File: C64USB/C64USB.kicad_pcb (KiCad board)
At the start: 2 copper layers, 39.3 x 64.2 mm, 32 parts, among them J2 USB_B, J3 AVR-ISP-6, J4 Joystick1, J5 Joystick2, J6 LED, U2 ATmega88-20A, Y1 16MHz

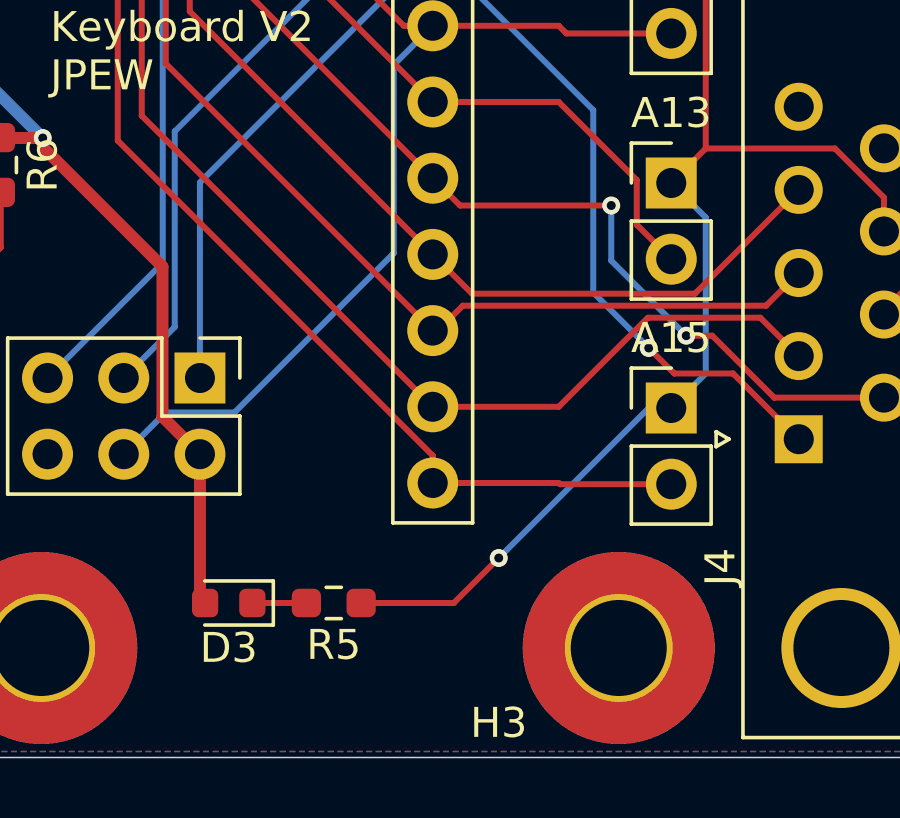
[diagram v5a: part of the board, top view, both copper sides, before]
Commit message: Remove debug LED
The debug LED isn't particularly useful since it's tied to the AUX line
and I didn't even bother populating it on the prototype board
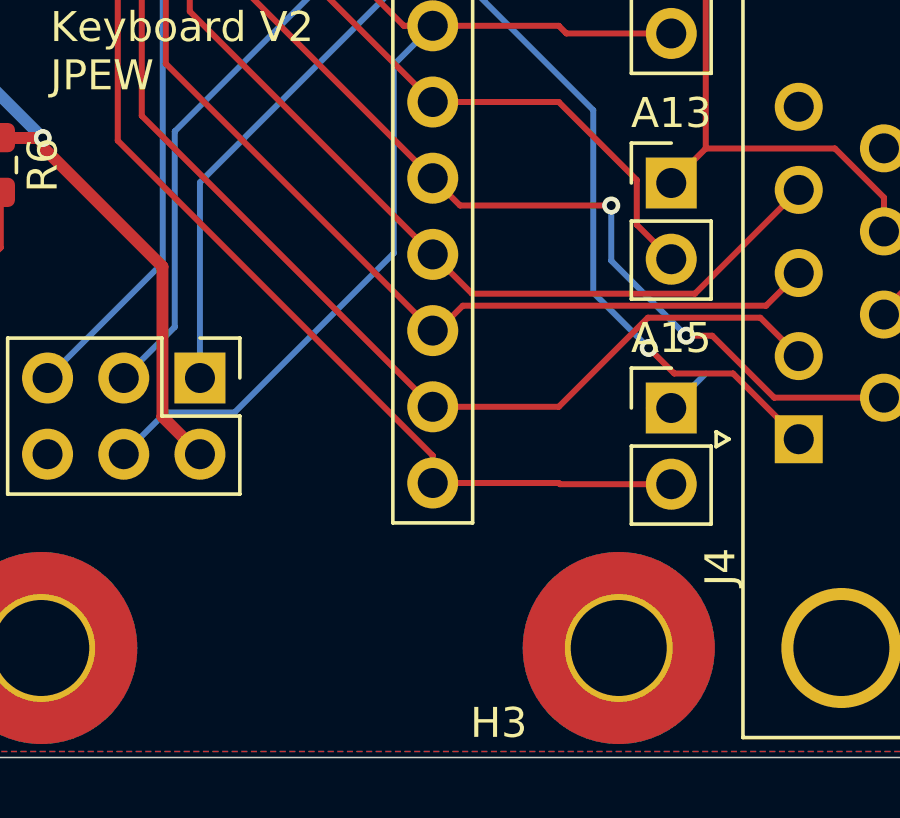
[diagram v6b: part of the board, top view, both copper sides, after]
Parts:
- removed D3: LED, LED_SMD:LED_0603_1608Metric
- removed R5: 120, Resistor_SMD:R_0603_1608Metric_Pad0.98x0.95mm_HandSolder
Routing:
- net /AUX: track 96.5 -> 77.4 mm, vias 2 -> 1
- net /PWR: track 143.7 -> 138.7 mm
- net Net-(D3-K): track 1.80 -> 0.00 mm

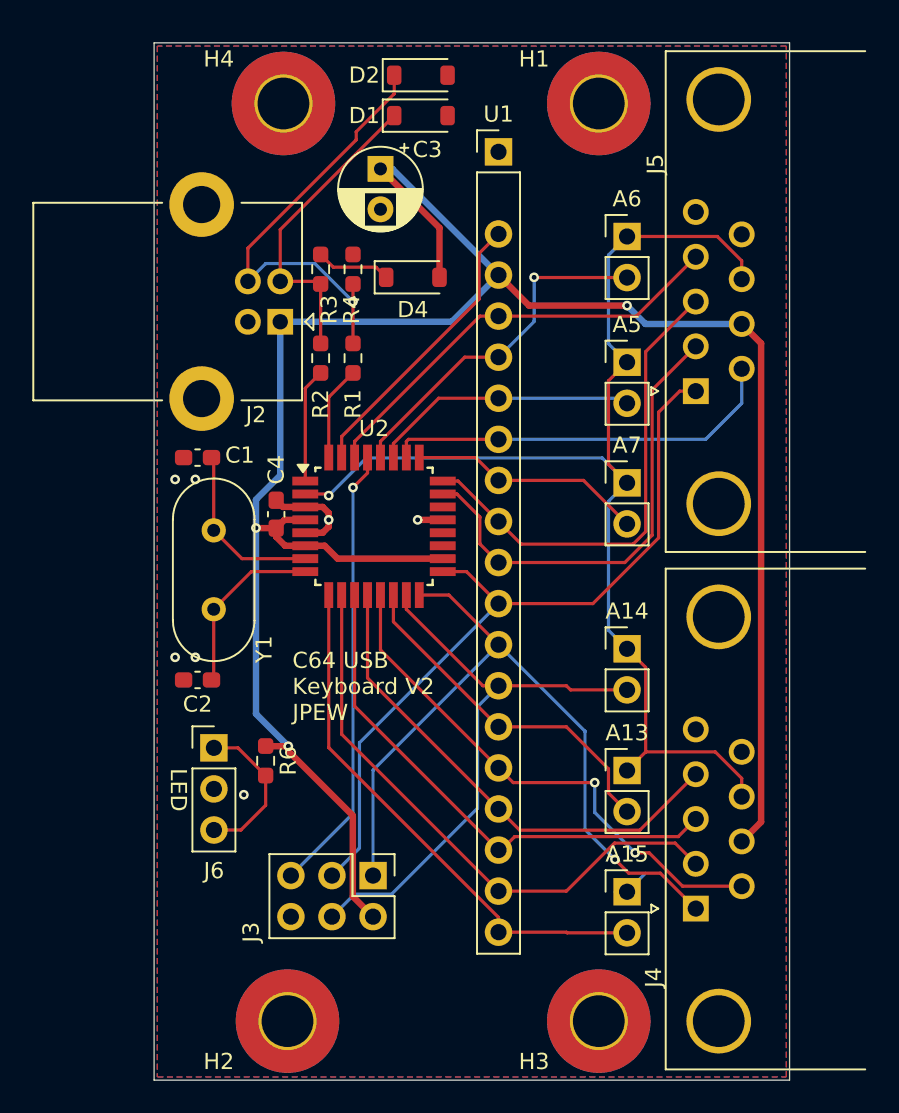
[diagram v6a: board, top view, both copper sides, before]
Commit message: Move mounting holes
Moves the mounting holes to a better position
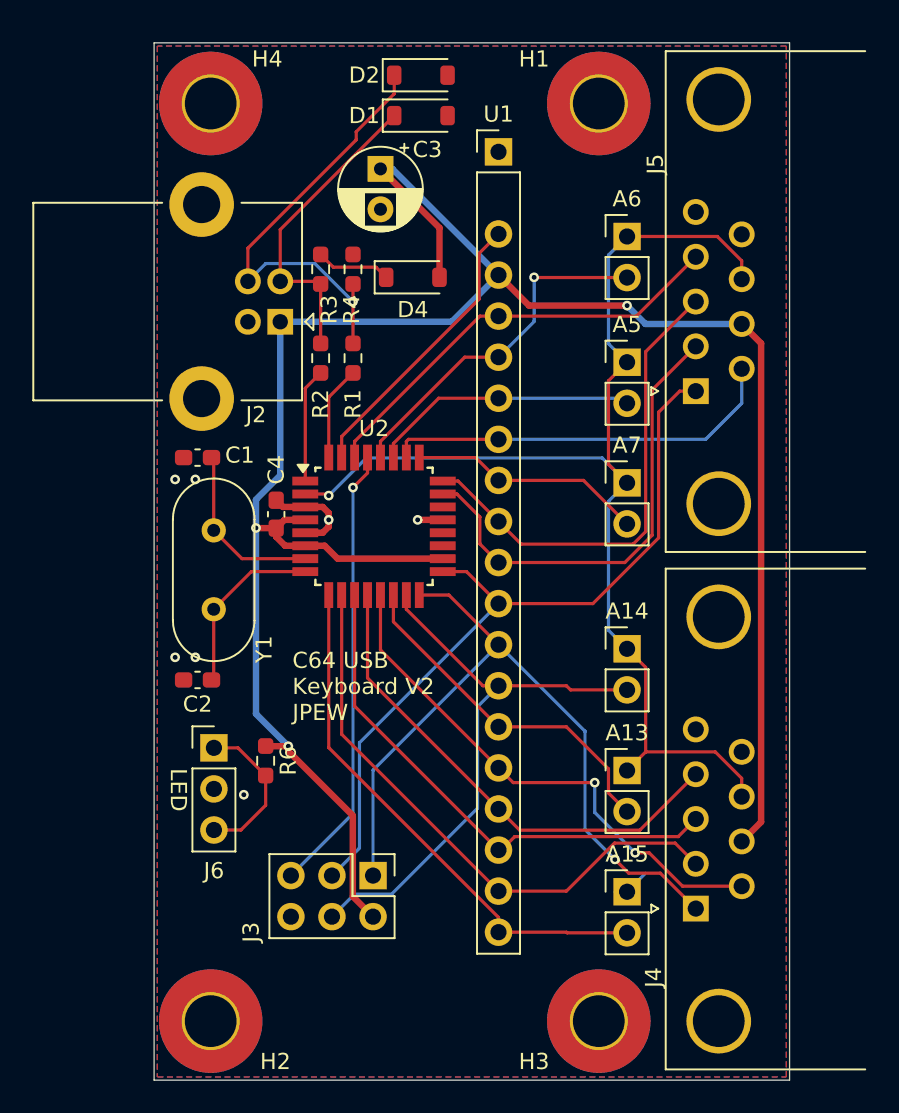
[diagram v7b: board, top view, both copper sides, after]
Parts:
- moved H2 4.75 mm to (117.0, 113.5)
- moved H4 4.50 mm to (117.0, 56.8)
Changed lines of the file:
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@@
 	(footprint "MountingHole:MountingHole_3.2mm_M3_Pad_TopBottom"
 		(layer "F.Cu")
-		(at 121.5 56.75)
+		(at 117 56.75)
 		(descr "Mounting Hole 3.2mm, M3")
 		(tags "mounting hole 3.2mm m3")
 		(property "Reference" "H4"
-			(at -4 -2.75 0)
+			(at 3.5 -2.75 0)
 			(layer "F.SilkS")
 			(effects
@@
 	(footprint "MountingHole:MountingHole_3.2mm_M3_Pad_TopBottom"
 		(layer "F.Cu")
-		(at 121.75 113.5)
+		(at 117 113.5)
 		(descr "Mounting Hole 3.2mm, M3")
 		(tags "mounting hole 3.2mm m3")
 		(property "Reference" "H2"
-			(at -4.25 2.5 0)
-			(layer "F.SilkS")
-			(effects
+			(at 4 2.5 0)
+			(layer "F.SilkS")
+			(effects

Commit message: Use buffer on joystick and aux keys
There was a problem where joystick or auxiliary key inputs would result
in keyboard keys being detected when they were not actually pressed.
While this is accurate to the actual Commodore 64 keyboard and joystick
input, having it happen on this USB device meant that it could not be
correctly disambiguated by the emulator. As such, the board is
redesigned to use a 74HCT541 tri state buffer chip to isolate the
Joystick and auxiliary inputs from the keyboard. It is still possible
that keyboard inputs can incorrectly show up as joystick movement, but
this is much less likely to cause a problem.

With the board redesign, the clearance around the keyboard header was
also increased to allow it to fit, and the USB connector was changed
from a micro-USB connector to a USB-B connector (I had too much trouble
hand soldering the micro USB connector).
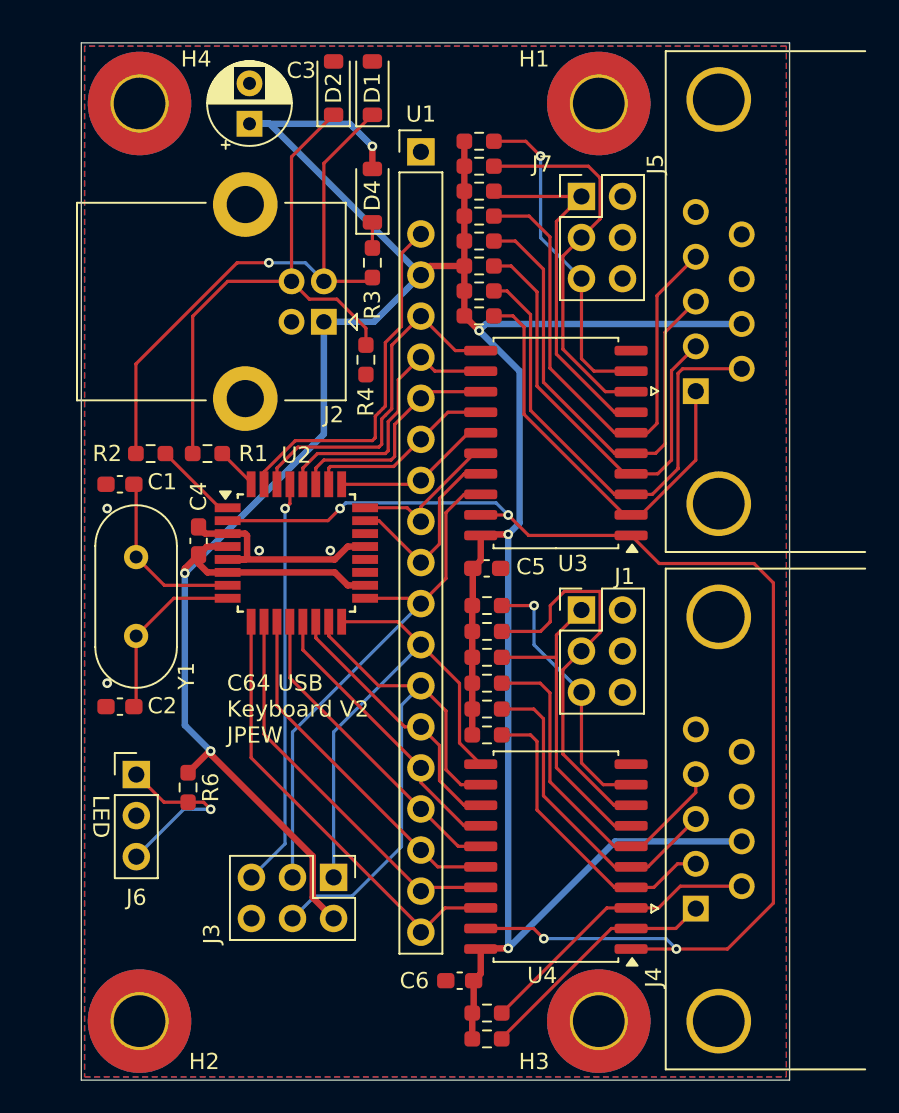
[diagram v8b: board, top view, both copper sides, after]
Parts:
- removed A13, A14, A15, A5, A6, A7: ~, Connector_PinHeader_2.54mm:PinHeader_1x02_P2.54mm_Vertical
- added C5: 100nF, Capacitor_SMD:C_0603_1608Metric_Pad1.08x0.95mm_HandSolder, F.Cu at (134.1, 85.5)
- added C6: 100nF, Capacitor_SMD:C_0603_1608Metric_Pad1.08x0.95mm_HandSolder, F.Cu at (132.4, 111.0)
- added J1: Conn_02x03_Odd_Even, Connector_PinHeader_2.54mm:PinHeader_2x03_P2.54mm_Vertical, F.Cu at (139.9, 88.1)
- added J7: Conn_02x03_Odd_Even, Connector_PinHeader_2.54mm:PinHeader_2x03_P2.54mm_Vertical, F.Cu at (139.9, 62.5)
- added R10: 10k, Resistor_SMD:R_0603_1608Metric_Pad0.98x0.95mm_HandSolder, F.Cu at (133.6, 63.7)
- added R11: 10k, Resistor_SMD:R_0603_1608Metric_Pad0.98x0.95mm_HandSolder, F.Cu at (133.6, 62.2)
- added R12: 10k, Resistor_SMD:R_0603_1608Metric_Pad0.98x0.95mm_HandSolder, F.Cu at (133.6, 60.6)
- added R13: 10k, Resistor_SMD:R_0603_1608Metric_Pad0.98x0.95mm_HandSolder, F.Cu at (133.6, 59.1)
- added R14: 10k, Resistor_SMD:R_0603_1608Metric_Pad0.98x0.95mm_HandSolder, F.Cu at (134.1, 114.6)
- added R15: 10k, Resistor_SMD:R_0603_1608Metric_Pad0.98x0.95mm_HandSolder, F.Cu at (134.1, 113.0)
- added R16: 10k, Resistor_SMD:R_0603_1608Metric_Pad0.98x0.95mm_HandSolder, F.Cu at (134.1, 95.8)
- added R17: 10k, Resistor_SMD:R_0603_1608Metric_Pad0.98x0.95mm_HandSolder, F.Cu at (134.1, 94.2)
- added R18: 10k, Resistor_SMD:R_0603_1608Metric_Pad0.98x0.95mm_HandSolder, F.Cu at (134.1, 92.6)
- added R19: 10k, Resistor_SMD:R_0603_1608Metric_Pad0.98x0.95mm_HandSolder, F.Cu at (134.1, 91.0)
- added R20: 10k, Resistor_SMD:R_0603_1608Metric_Pad0.98x0.95mm_HandSolder, F.Cu at (134.1, 89.4)
- added R21: 10k, Resistor_SMD:R_0603_1608Metric_Pad0.98x0.95mm_HandSolder, F.Cu at (134.1, 87.8)
- added R5: 10k, Resistor_SMD:R_0603_1608Metric_Pad0.98x0.95mm_HandSolder, F.Cu at (133.6, 69.9)
- added R7: 10k, Resistor_SMD:R_0603_1608Metric_Pad0.98x0.95mm_HandSolder, F.Cu at (133.6, 66.8)
- added R8: 10k, Resistor_SMD:R_0603_1608Metric_Pad0.98x0.95mm_HandSolder, F.Cu at (133.6, 68.3)
- added R9: 10k, Resistor_SMD:R_0603_1608Metric_Pad0.98x0.95mm_HandSolder, F.Cu at (133.6, 65.3)
- added U3: 74HCT541, Package_SO:SOIC-20W_7.5x12.8mm_P1.27mm, F.Cu at (138.3, 77.7)
- added U4: 74HCT541, Package_SO:SOIC-20W_7.5x12.8mm_P1.27mm, F.Cu at (138.3, 103.3)
- moved R2 12.1 mm to (113.3, 78.4), turned to 180 degrees
- moved R1 10.8 mm to (116.8, 78.4), turned to 180 degrees
- moved C3 8.57 mm to (119.4, 58.0), turned to 90 degrees
- moved R4 5.66 mm to (126.6, 72.6), turned to 90 degrees
- moved D4 5.63 mm to (127.0, 62.5), turned to 90 degrees
- moved D2 5.46 mm to (124.6, 55.8), turned to 90 degrees
- moved R6 5.08 mm to (115.6, 99.0)
- moved J6 5.08 mm to (112.4, 98.2)
- moved Y1 5.08 mm to (112.4, 89.7)
- moved C1 5.08 mm to (111.4, 80.3)
- moved C2 5.08 mm to (111.4, 94.0)
- moved C4 5.08 mm to (116.2, 83.8)
- moved U2 5.08 mm to (122.3, 84.5)
- moved U1 4.80 mm to (130.0, 59.7)
- moved H2 4.40 mm to (112.6, 113.5)
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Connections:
- J4 pad 1: /ROW_0 -> /JOY_1_1
- J4 pad 2: /ROW_1 -> /JOY_1_2
- J4 pad 3: /ROW_2 -> /JOY_1_3
- J4 pad 4: /ROW_3 -> /JOY_1_4
- J4 pad 6: /ROW_4 -> /JOY_1_6
- J4 pad 8: /AUX -> GNDREF
- J5 pad 1: /COL_0 -> /JOY_2_1
- J5 pad 2: /COL_1 -> /JOY_2_2
- J5 pad 3: /COL_2 -> /JOY_2_3
- J5 pad 4: /COL_3 -> /JOY_2_4
- J5 pad 6: /COL_4 -> /JOY_2_6
- J5 pad 8: /AUX -> GNDREF
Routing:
- net /PWR: track 138.7 -> 202.3 mm, vias 3 -> 6
- net /JOY_2_4: track 0.00 -> 31.9 mm
- net /JOY_2_6: track 0.00 -> 30.7 mm
- net /JOY_2_3: track 0.00 -> 29.9 mm
- net /JOY_2_2: track 0.00 -> 27.7 mm
- net /JOY_2_1: track 0.00 -> 26.4 mm
- net /AUX_5: track 0.00 -> 24.2 mm
- net /AUX_2: track 0.00 -> 23.7 mm
- net /AUX_3: track 0.00 -> 22.1 mm
- net /JOY_1_4: track 0.00 -> 21.9 mm
- net /AUX_1: track 0.00 -> 20.2 mm, vias 0 -> 1
- net /COL_2: track 30.0 -> 9.78 mm
- net /JOY_1_3: track 0.00 -> 20.1 mm
- net /AUX_6: track 0.00 -> 19.9 mm
- net /JOY_1_2: track 0.00 -> 19.0 mm
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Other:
- board size 39.3 x 64.2 mm -> 43.8 x 64.2 mm
